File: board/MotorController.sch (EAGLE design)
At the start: 39 parts, among them IC1 ATMEGA328P-PU, Q1 BT137-600E, Q2 IPP80P03P4L-04, Q3 SUP75P03-07-H-NH, Y1 16Mhz

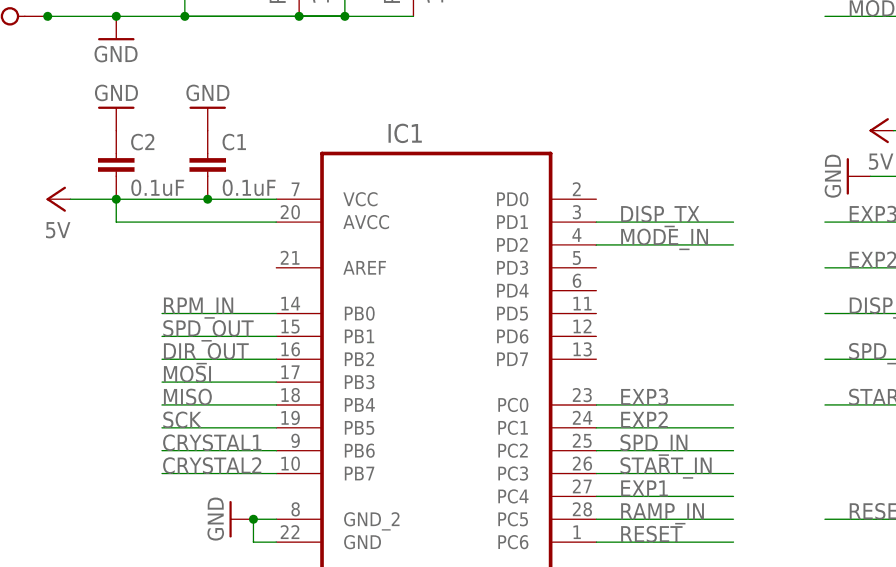
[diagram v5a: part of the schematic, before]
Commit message: Connect RPM IN to pin 5 which supports interrupts
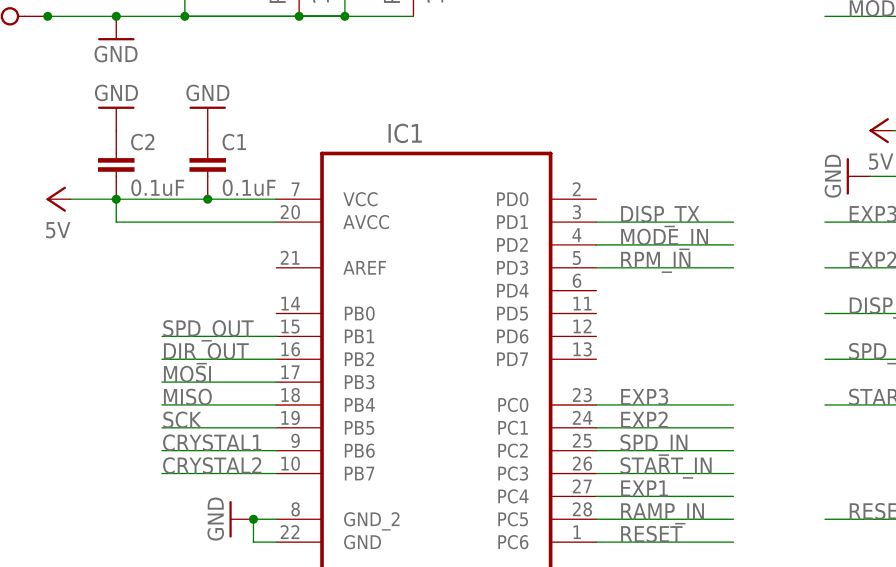
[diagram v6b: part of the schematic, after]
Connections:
- net RPM_IN: now also IC1.PD3; no longer IC1.PB0
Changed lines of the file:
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@@
 <layer number="113" name="IDFDebug" color="7" fill="1" visible="yes" active="yes"/>
 <layer number="116" name="Patch_BOT" color="9" fill="4" visible="yes" active="yes"/>
+<layer number="118" name="Rect_Pads" color="7" fill="1" visible="no" active="no"/>
 <layer number="121" name="_tsilk" color="7" fill="1" visible="yes" active="yes"/>
 <layer number="122" name="_bsilk" color="7" fill="1" visible="yes" active="yes"/>
@@
 <layer number="230" name="230bmp" color="7" fill="1" visible="yes" active="yes"/>
 <layer number="231" name="231bmp" color="7" fill="1" visible="yes" active="yes"/>
+<layer number="232" name="Eagle3D_PG2" color="7" fill="1" visible="no" active="no"/>
+<layer number="233" name="Eagle3D_PG3" color="7" fill="1" visible="no" active="no"/>
 <layer number="248" name="Housing" color="7" fill="1" visible="yes" active="yes"/>
 <layer number="249" name="Edge" color="7" fill="1" visible="yes" active="yes"/>
@@
 </segment>
 <segment>
-<pinref part="IC1" gate="A" pin="PB0"/>
-<wire x1="-22.86" y1="-10.16" x2="-35.56" y2="-10.16" width="0.1524" layer="91"/>
-<label x="-35.56" y="-10.16" size="1.778" layer="95"/>
-</segment>
-</net>
+<pinref part="IC1" gate="A" pin="PD3"/>
+<wire x1="12.7" y1="-5.08" x2="27.94" y2="-5.08" width="0.1524" layer="91"/>
+<label x="15.24" y="-5.08" size="1.778" layer="95"/>
+</segment>
+</net>

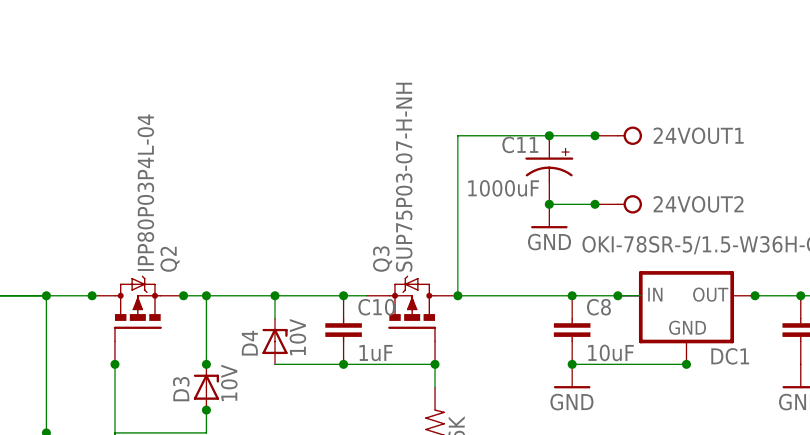
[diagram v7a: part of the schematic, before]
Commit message: Switched to 60V MOSFETs and updated BOM and inventory
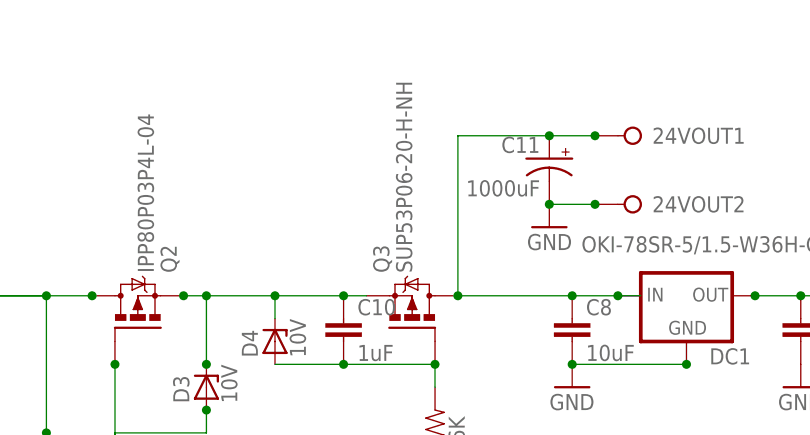
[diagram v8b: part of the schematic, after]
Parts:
- Q2: device SaintGimp:IPP80P03P4L-04-H-NH -> SaintGimp:SUP53P06-20-H-NH
- Q3: value SUP75P03-07-H-NH -> SUP53P06-20-H-NH; device SaintGimp:SUP75P03-07-H-NH -> SaintGimp:SUP53P06-20-H-NH
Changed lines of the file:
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@@
 <part name="C5" library="SaintGimp" deviceset="CAPACITOR-*" device="2.5MM" value="0.1uF"/>
 <part name="R5" library="SaintGimp" deviceset="RESISTOR-*" device="7.5MM" value="1K"/>
-<part name="Q2" library="SaintGimp" deviceset="IPP80P03P4L-04" device="-H-NH" value="IPP80P03P4L-04"/>
+<part name="Q2" library="SaintGimp" deviceset="SUP53P06-20" device="-H-NH" value="IPP80P03P4L-04"/>
 <part name="R8" library="SaintGimp" deviceset="RESISTOR-*" device="7.5MM" value="10K"/>
 <part name="D3" library="SaintGimp" deviceset="ZENER" device="-7.5" value="10V"/>
@@
 <part name="5V7" library="SaintGimp" deviceset="VCC" device="" value="5V"/>
 <part name="GND18" library="SaintGimp" deviceset="GND" device=""/>
-<part name="Q3" library="SaintGimp" deviceset="SUP75P03-07" device="-H-NH" value="SUP75P03-07-H-NH"/>
+<part name="Q3" library="SaintGimp" deviceset="SUP53P06-20" device="-H-NH" value="SUP53P06-20-H-NH"/>
 <part name="R7" library="SaintGimp" deviceset="RESISTOR-*" device="7.5MM" value="576K"/>
 <part name="GND19" library="SaintGimp" deviceset="GND" device=""/>
